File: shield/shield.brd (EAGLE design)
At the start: 68.6 x 53.3 mm, 23 parts, among them IC1 MCP2515-E/SO, IC2 MCP2562, IC3 LM2595NDH

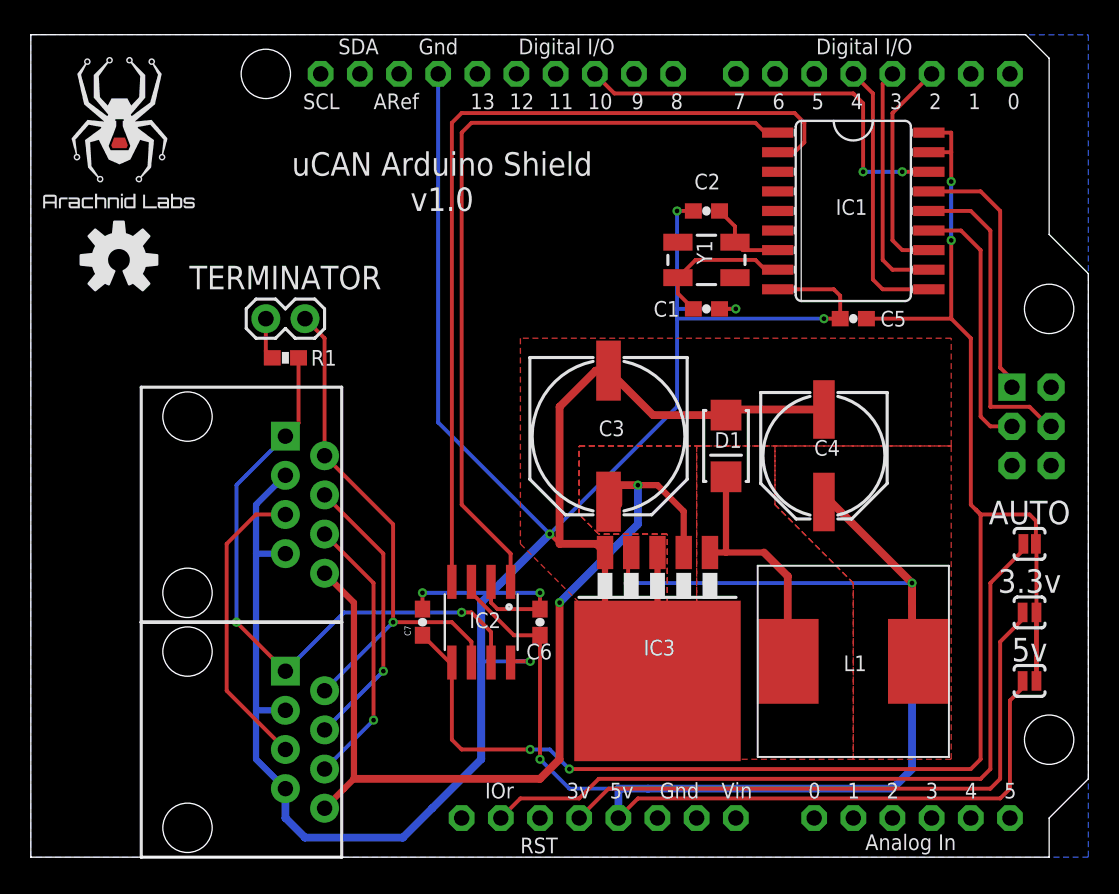
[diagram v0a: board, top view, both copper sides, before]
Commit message: Switch to split termination with a switch
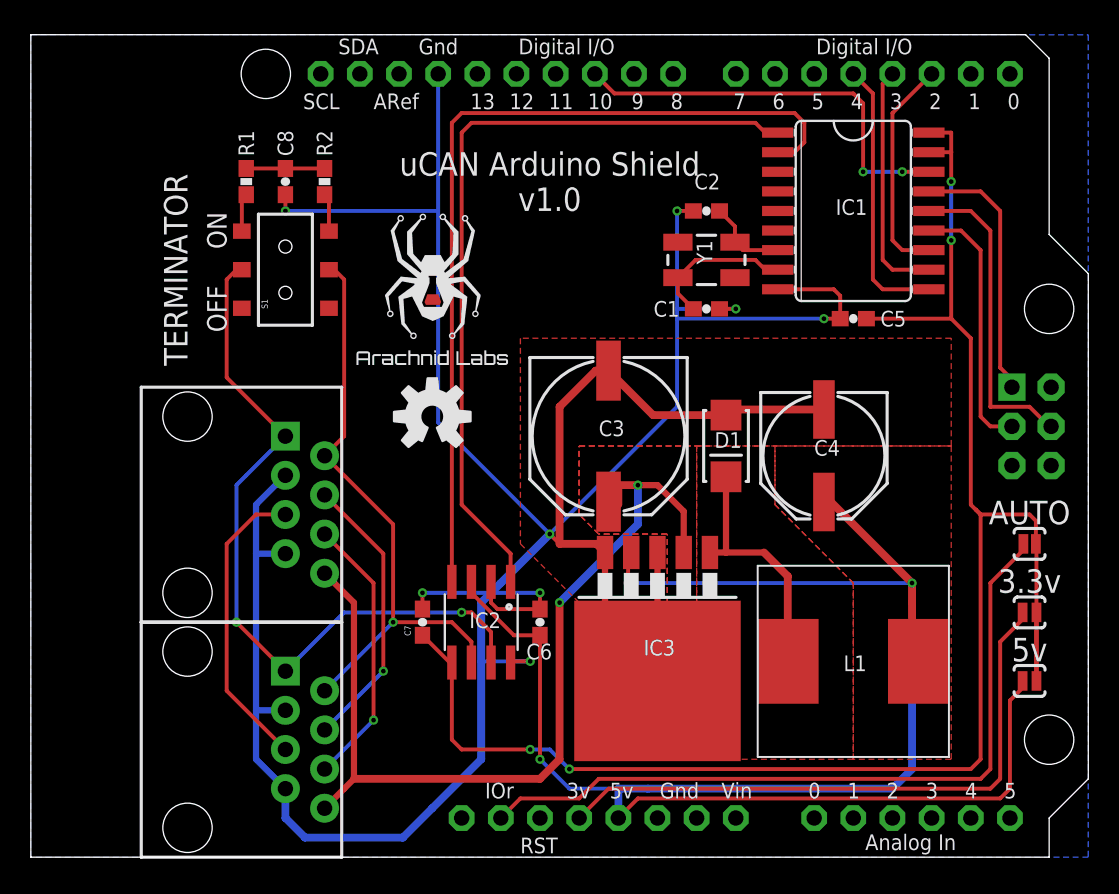
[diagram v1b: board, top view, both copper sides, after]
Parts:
- removed JP1: (no value), SparkFun-Passives:1X02
- added C8: 4.7nF, SparkFun-Passives:0603-CAP
- added R2: 60, SparkFun-Passives:0603-RES
- added S1: DPDT, SparkFun-Electromechanical:AYZ0202
- R1: value 120 -> 60
- moved U$4 22.7 mm to (26.0, 36.8)
- moved U$5 22.7 mm to (26.0, 28.6)
- moved R1 11.7 mm to (14.0, 43.8), turned to 270 degrees
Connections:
- new net N$2: R1.2, S1.3
- new net N$3: R2.2, S1.6
- net CANH: now also S1.2; no longer R1.2
- net CANL: now also S1.5; no longer JP1.1
- net GND: now also C8.2
- net N$7: now also C8.1, R2.1; no longer JP1.2
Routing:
- net GND: track 210.0 -> 221.0 mm, vias 7 -> 8
- net CANH: track 40.7 -> 48.3 mm
- net CANL: track 35.3 -> 39.1 mm
- net N$3: track 0.00 -> 2.48 mm
- net N$2: track 0.00 -> 2.48 mm
- net N$7: track 2.71 -> 5.08 mm
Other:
- board text added: "OFF"
- board text added: "ON"
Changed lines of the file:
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@@
 <board>
 <plain>
-<text x="16.51" y="36.83" size="1.524" layer="25" font="vector" ratio="10" align="bottom-center">TERMINATOR</text>
+<text x="10.16" y="38.1" size="1.524" layer="25" font="vector" ratio="10" rot="R90" align="bottom-center">TERMINATOR</text>
 <text x="64.77" y="21.59" size="1.524" layer="25" font="vector" ratio="10" align="bottom-center">AUTO</text>
 <text x="64.77" y="17.145" size="1.524" layer="25" font="vector" ratio="10" align="bottom-center">3.3v</text>
@@
 <hole x="66.04" y="35.56" drill="3.2"/>
 <hole x="66.04" y="7.62" drill="3.2"/>
-<text x="26.67" y="41.91" size="1.524" layer="25" font="vector" ratio="10" align="bottom-center">uCAN Arduino Shield
+<text x="33.655" y="41.91" size="1.524" layer="25" font="vector" ratio="10" align="bottom-center">uCAN Arduino Shield
 v1.0</text>
+<text x="12.7" y="40.64" size="1.27" layer="25" ratio="10" rot="R90" align="bottom-center">ON</text>
+<text x="12.7" y="35.56" size="1.27" layer="25" ratio="10" rot="R90" align="bottom-center">OFF</text>
 </plain>
 <attributes>
@@
 <element name="U$2" library="SparkFun-Connectors" package="RJ45-8" value="RJ45-8PTH" x="10.16" y="22.86" rot="R270"/>
 <element name="U$3" library="SparkFun-Connectors" package="RJ45-8" value="RJ45-8PTH" x="10.16" y="7.62" rot="R270"/>
-<element name="JP1" library="SparkFun-Passives" package="1X02" value="" x="17.78" y="34.925" smashed="yes" rot="R180">
-<attribute name="VALUE" x="19.05" y="38.1" size="1.27" layer="27" rot="R180"/>
-</element>
-<element name="R1" library="SparkFun-Passives" package="0603-RES" value="120" x="16.51" y="32.385" smashed="yes">
-<attribute name="NAME" x="18.161" y="31.877" size="1.016" layer="25" font="vector" ratio="15"/>
+<element name="R1" library="SparkFun-Passives" package="0603-RES" value="60" x="13.97" y="43.815" smashed="yes" rot="R270">
+<attribute name="NAME" x="14.478" y="45.466" size="1.016" layer="25" font="vector" ratio="15" rot="R90"/>
 </element>
 <element name="SJ1" library="SparkFun-Passives" package="SJ_2S-NOTRACE" value="SOLDERJUMPERNC2" x="64.77" y="20.32" smashed="yes"/>
 <element name="SJ2" library="SparkFun-Passives" package="SJ_2S-NO" value="SOLDERJUMPERNO" x="64.77" y="11.43" smashed="yes"/>
 <element name="SJ3" library="SparkFun-Passives" package="SJ_2S-NO" value="SOLDERJUMPERNO" x="64.77" y="15.875" smashed="yes"/>
-<element name="U$4" library="nickparts" package="ARACHNID_LABS_LOGO_SM" value="" x="5.715" y="46.99"/>
-<element name="U$5" library="SparkFun-Aesthetics" package="OSHW-LOGO-M" value="" x="5.715" y="38.735"/>
+<element name="U$4" library="nickparts" package="ARACHNID_LABS_LOGO_SM" value="" x="26.035" y="36.83"/>
+<element name="U$5" library="SparkFun-Aesthetics" package="OSHW-LOGO-M" value="" x="26.035" y="28.575"/>
 <element name="C7" library="SparkFun-Passives" package="0603-CAP" value="0.1u" x="25.4" y="15.24" rot="R90"/>
+<element name="S1" library="SparkFun-Electromechanical" package="AYZ0202" value="DPDT" x="16.51" y="38.1" rot="R90">
+<attribute name="PROD_ID" value="SWCH-08179" x="16.51" y="38.1" size="1.778" layer="27" rot="R90" display="off"/>
+</element>
+<element name="R2" library="SparkFun-Passives" package="0603-RES" value="60" x="19.05" y="43.815" smashed="yes" rot="R270">
+<attribute name="NAME" x="19.558" y="45.466" size="1.016" layer="25" font="vector" ratio="15" rot="R90"/>
+</element>
+<element name="C8" library="SparkFun-Passives" package="0603-CAP" value="4.7nF" x="16.51" y="43.815" smashed="yes" rot="R270">
+<attribute name="NAME" x="17.018" y="45.466" size="1.016" layer="25" font="vector" ratio="15" rot="R90"/>
+</element>
 </elements>
 <signals>
@@
 <wire x1="51.435" y1="34.925" x2="41.91" y2="34.925" width="0.254" layer="16"/>
 <wire x1="52.49" y1="36.41" x2="52.49" y2="34.925" width="0.254" layer="1"/>
-<wire x1="26.416" y1="50.8" x2="26.416" y2="28.194" width="0.254" layer="16"/>
+<wire x1="26.416" y1="50.8" x2="26.416" y2="41.91" width="0.254" layer="16"/>
+<wire x1="26.416" y1="41.91" x2="26.416" y2="28.194" width="0.254" layer="16"/>
 <wire x1="26.416" y1="28.194" x2="33.655" y2="20.955" width="0.254" layer="16"/>
 <wire x1="33.02" y1="16.09" x2="33.02" y2="17.145" width="0.254" layer="1"/>
@@
 <via x="25.4" y="17.145" extent="1-16" drill="0.3"/>
 <wire x1="25.4" y1="17.145" x2="29.845" y2="17.145" width="0.254" layer="16"/>
+<contactref element="C8" pad="2"/>
+<wire x1="16.51" y1="42.965" x2="16.51" y2="41.91" width="0.254" layer="1"/>
+<via x="16.51" y="41.91" extent="1-16" drill="0.3"/>
+<wire x1="16.51" y1="41.91" x2="26.416" y2="41.91" width="0.254" layer="16"/>
 </signal>
 <signal name="N$6">
@@
 <contactref element="U$2" pad="1"/>
 <contactref element="U$3" pad="1"/>
-<contactref element="R1" pad="2"/>
 <wire x1="16.51" y1="27.305" x2="13.97" y2="24.765" width="0.254" layer="16"/>
 <wire x1="13.97" y1="24.765" x2="13.335" y2="24.13" width="0.254" layer="16"/>
@@
 <via x="13.335" y="15.24" extent="1-16" drill="0.3"/>
 <wire x1="13.335" y1="15.24" x2="16.51" y2="12.065" width="0.254" layer="1"/>
-<wire x1="17.36" y1="32.385" x2="17.36" y2="28.155" width="0.254" layer="1"/>
-<wire x1="17.36" y1="28.155" x2="16.51" y2="27.305" width="0.254" layer="1"/>
 <wire x1="20.32" y1="15.875" x2="16.51" y2="12.065" width="0.254" layer="16"/>
 <wire x1="29.845" y1="12.6238" x2="29.845" y2="14.605" width="0.254" layer="1"/>
@@
 <via x="27.94" y="15.875" extent="1-16" drill="0.3"/>
 <wire x1="27.94" y1="15.875" x2="20.32" y2="15.875" width="0.254" layer="16"/>
+<contactref element="S1" pad="2"/>
+<wire x1="13.685" y1="38.1" x2="13.335" y2="38.1" width="0.254" layer="1"/>
+<wire x1="13.335" y1="38.1" x2="12.7" y2="37.465" width="0.254" layer="1"/>
+<wire x1="12.7" y1="37.465" x2="12.7" y2="31.115" width="0.254" layer="1"/>
+<wire x1="12.7" y1="31.115" x2="16.51" y2="27.305" width="0.254" layer="1"/>
 </signal>
 <signal name="CANL">
@@
 <contactref element="U$2" pad="2"/>
 <contactref element="U$3" pad="2"/>
-<contactref element="JP1" pad="1"/>
 <wire x1="19.05" y1="26.035" x2="23.495" y2="21.59" width="0.254" layer="1"/>
 <wire x1="23.495" y1="21.59" x2="23.495" y2="15.24" width="0.254" layer="1"/>
 <via x="23.495" y="15.24" extent="1-16" drill="0.3"/>
-<wire x1="17.78" y1="34.925" x2="19.05" y2="33.655" width="0.254" layer="1"/>
-<wire x1="19.05" y1="33.655" x2="19.05" y2="26.035" width="0.254" layer="1"/>
 <wire x1="28.575" y1="12.6238" x2="28.575" y2="13.97" width="0.254" layer="1"/>
 <wire x1="28.575" y1="13.97" x2="27.305" y2="15.24" width="0.254" layer="1"/>
 <wire x1="27.305" y1="15.24" x2="23.495" y2="15.24" width="0.254" layer="1"/>
 <wire x1="23.495" y1="15.24" x2="19.05" y2="10.795" width="0.254" layer="16"/>
+<contactref element="S1" pad="5"/>
+<wire x1="19.335" y1="38.1" x2="19.685" y2="38.1" width="0.254" layer="1"/>
+<wire x1="19.685" y1="38.1" x2="20.32" y2="37.465" width="0.254" layer="1"/>
+<wire x1="20.32" y1="37.465" x2="20.32" y2="27.305" width="0.254" layer="1"/>
+<wire x1="20.32" y1="27.305" x2="19.05" y2="26.035" width="0.254" layer="1"/>
 </signal>
 <signal name="VIN">
@@
 <via x="22.225" y="8.89" extent="1-16" drill="0.3"/>
 <wire x1="22.225" y1="8.89" x2="19.05" y2="5.715" width="0.254" layer="16"/>
-</signal>
-<signal name="N$7">
-<contactref element="JP1" pad="2"/>
-<contactref element="R1" pad="1"/>
-<wire x1="15.24" y1="34.925" x2="15.24" y2="32.805" width="0.254" layer="1"/>
-<wire x1="15.24" y1="32.805" x2="15.66" y2="32.385" width="0.254" layer="1"/>
 </signal>
 <signal name="RX1_BF">
@@
 <wire x1="61.595" y1="22.225" x2="61.2775" y2="22.5425" width="0.254" layer="1"/>
 </signal>
+<signal name="N$7">
+<contactref element="R1" pad="1"/>
+<contactref element="C8" pad="1"/>
+<contactref element="R2" pad="1"/>
+<wire x1="13.97" y1="44.665" x2="16.51" y2="44.665" width="0.254" layer="1"/>
+<wire x1="19.05" y1="44.665" x2="16.51" y2="44.665" width="0.254" layer="1"/>
+</signal>
+<signal name="N$2">
+<contactref element="S1" pad="3"/>
+<contactref element="R1" pad="2"/>
+<wire x1="13.685" y1="40.6" x2="13.685" y2="42.68" width="0.254" layer="1"/>
+<wire x1="13.685" y1="42.68" x2="13.97" y2="42.965" width="0.254" layer="1"/>
+</signal>
+<signal name="N$3">
+<contactref element="S1" pad="6"/>
+<contactref element="R2" pad="2"/>
+<wire x1="19.335" y1="40.6" x2="19.335" y2="42.68" width="0.254" layer="1"/>
+<wire x1="19.335" y1="42.68" x2="19.05" y2="42.965" width="0.254" layer="1"/>
+</signal>
 </signals>

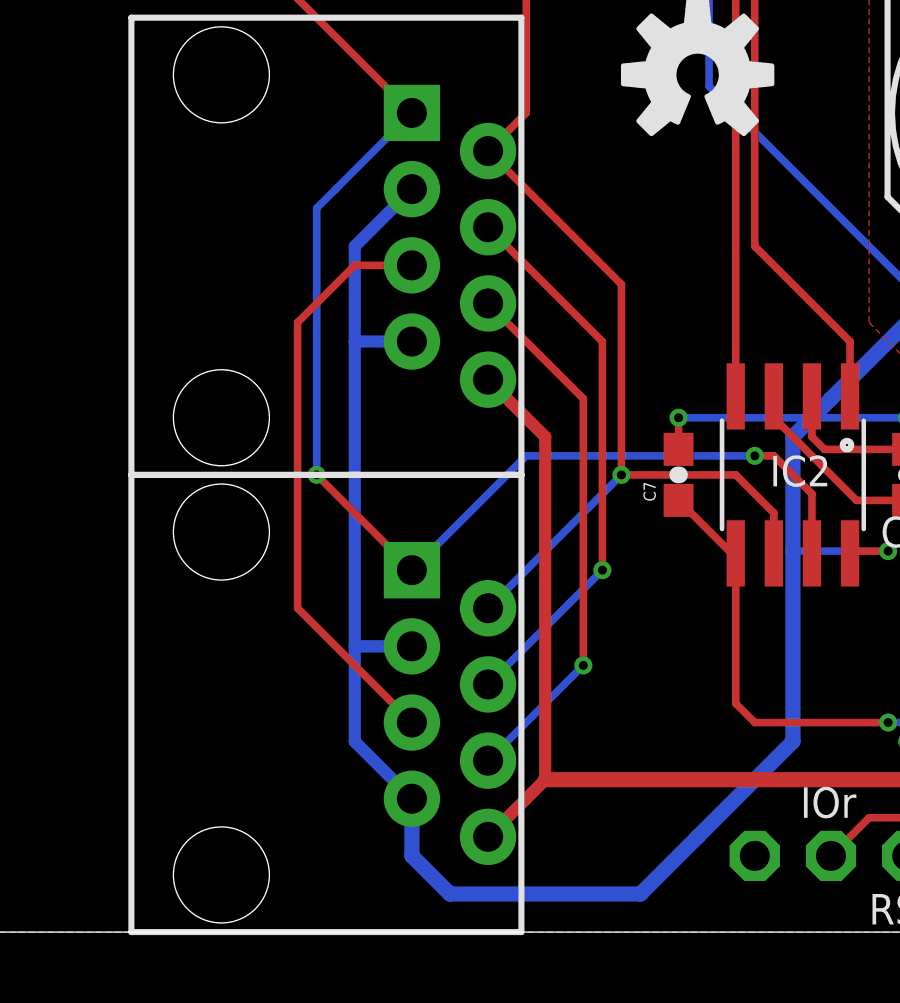
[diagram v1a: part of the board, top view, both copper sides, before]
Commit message: Modify injector for split termination
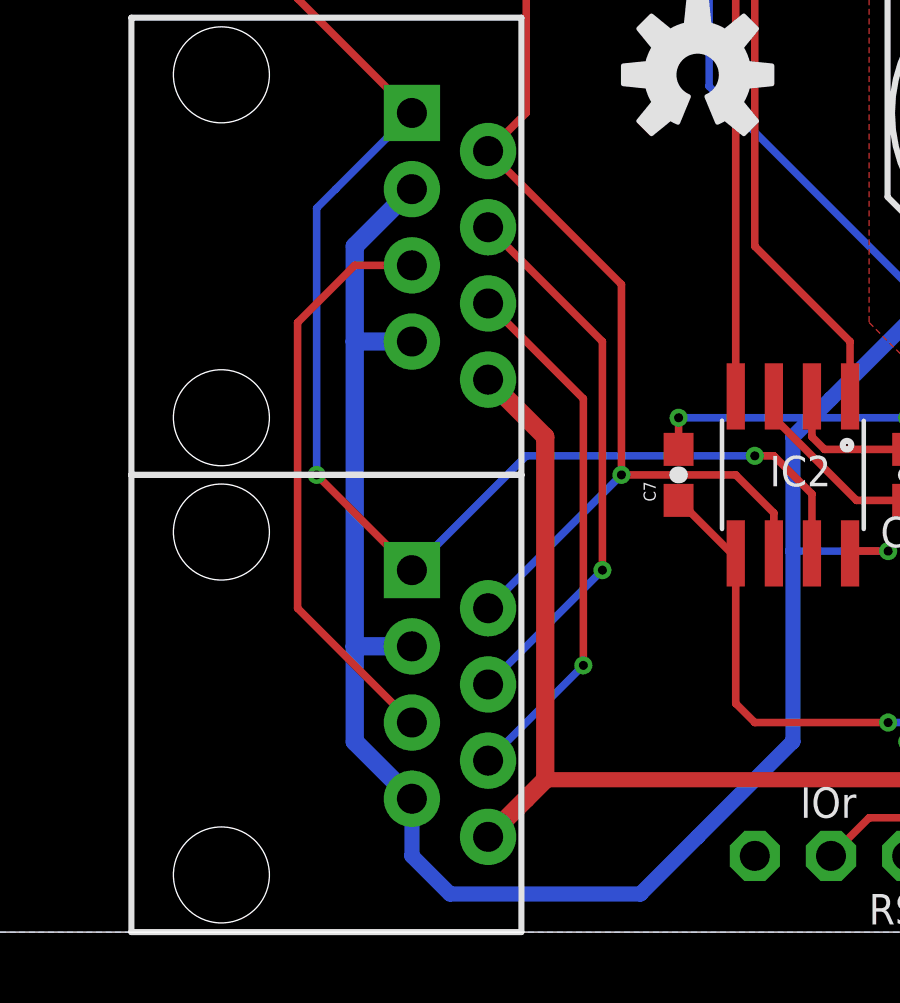
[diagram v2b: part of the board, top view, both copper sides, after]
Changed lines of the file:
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@@
 <contactref element="U$2" pad="7"/>
 <contactref element="U$3" pad="7"/>
-<wire x1="16.51" y1="24.765" x2="14.605" y2="22.86" width="0.4064" layer="16"/>
-<wire x1="14.605" y1="22.86" x2="14.605" y2="19.685" width="0.4064" layer="16"/>
-<wire x1="14.605" y1="19.685" x2="14.605" y2="9.525" width="0.4064" layer="16"/>
-<wire x1="14.605" y1="9.525" x2="14.605" y2="6.35" width="0.4064" layer="16"/>
-<wire x1="14.605" y1="6.35" x2="16.51" y2="4.445" width="0.4064" layer="16"/>
-<wire x1="16.51" y1="9.525" x2="14.605" y2="9.525" width="0.4064" layer="16"/>
-<wire x1="16.51" y1="19.685" x2="14.605" y2="19.685" width="0.4064" layer="16"/>
+<wire x1="16.51" y1="24.765" x2="14.605" y2="22.86" width="0.6096" layer="16"/>
+<wire x1="14.605" y1="22.86" x2="14.605" y2="19.685" width="0.6096" layer="16"/>
+<wire x1="14.605" y1="19.685" x2="14.605" y2="9.525" width="0.6096" layer="16"/>
+<wire x1="14.605" y1="9.525" x2="14.605" y2="6.35" width="0.6096" layer="16"/>
+<wire x1="14.605" y1="6.35" x2="16.51" y2="4.445" width="0.6096" layer="16"/>
+<wire x1="16.51" y1="9.525" x2="14.605" y2="9.525" width="0.6096" layer="16"/>
+<wire x1="16.51" y1="19.685" x2="14.605" y2="19.685" width="0.6096" layer="16"/>
 <wire x1="40.64" y1="19.7612" x2="40.64" y2="11.43" width="0.4064" layer="1"/>
 <wire x1="37.2364" y1="19.7612" x2="37.2364" y2="14.8336" width="0.4064" layer="1"/>
@@
 <contactref element="U$2" pad="8"/>
 <contactref element="U$3" pad="8"/>
-<wire x1="19.05" y1="3.175" x2="20.32" y2="4.445" width="0.4064" layer="1"/>
-<wire x1="20.32" y1="4.445" x2="20.955" y2="5.08" width="0.4064" layer="1"/>
-<wire x1="20.955" y1="5.08" x2="20.955" y2="16.51" width="0.4064" layer="1"/>
-<wire x1="20.955" y1="16.51" x2="19.05" y2="18.415" width="0.4064" layer="1"/>
+<wire x1="19.05" y1="3.175" x2="20.32" y2="4.445" width="0.6096" layer="1"/>
+<wire x1="20.32" y1="4.445" x2="20.955" y2="5.08" width="0.6096" layer="1"/>
+<wire x1="20.955" y1="5.08" x2="20.955" y2="16.51" width="0.6096" layer="1"/>
+<wire x1="20.955" y1="16.51" x2="19.05" y2="18.415" width="0.6096" layer="1"/>
 <wire x1="42.3418" y1="19.7612" x2="42.3418" y2="22.4282" width="0.4064" layer="1"/>
 <wire x1="42.3418" y1="22.4282" x2="40.64" y2="24.13" width="0.4064" layer="1"/>
